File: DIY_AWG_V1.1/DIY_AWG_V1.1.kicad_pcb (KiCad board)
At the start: 4 copper layers, 100 x 100 mm, 0 parts

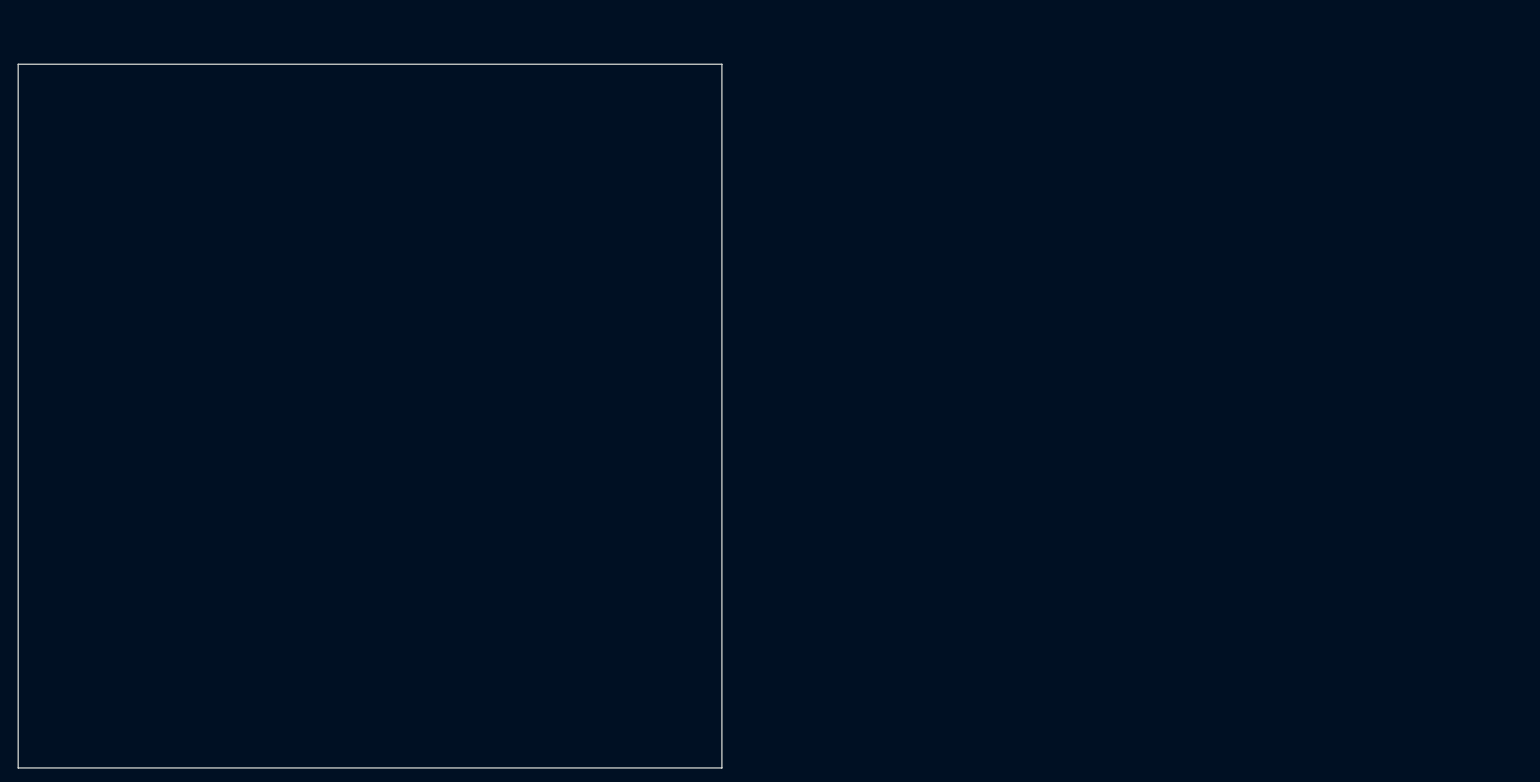
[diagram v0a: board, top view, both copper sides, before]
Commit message: Updated PCB design, uploaded necessary footprints and symbols for some components
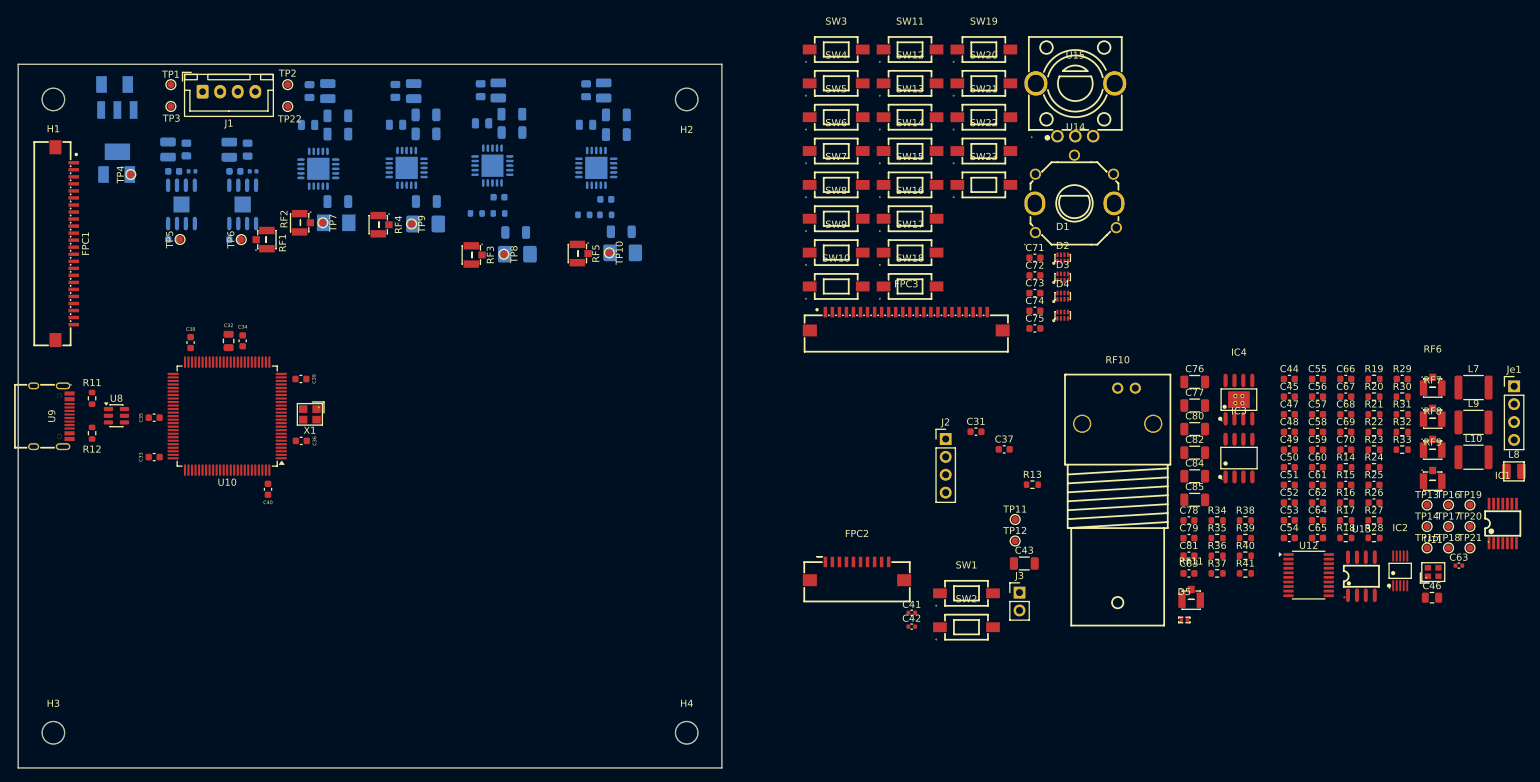
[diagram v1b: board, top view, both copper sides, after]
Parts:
- added C1: 22u, easyeda2kicad:CASE-B_3528, B.Cu at (84.2, 50.4)
- added C10: 4.7n, Capacitor_SMD:C_0402_1005Metric, B.Cu at (103.9, 62.7)
- added C11: 2.2u, Capacitor_SMD:C_0805_2012Metric, B.Cu at (111.7, 56.1)
- added C12: 22u, easyeda2kicad:CASE-B_3528, B.Cu at (84.5, 63.2)
- added C13: 10u, Capacitor_SMD:C_0603_1608Metric, B.Cu at (92.6, 72.4)
- added C14: 10u, Capacitor_SMD:C_0603_1608Metric, B.Cu at (101.3, 72.4)
- added C15: 22u, Capacitor_SMD:C_1206_3216Metric, B.Cu at (115.9, 67.0)
- added C16: 10n, Capacitor_SMD:C_0603_1608Metric, B.Cu at (138.8, 66.4)
- added C17: 22u, easyeda2kicad:CAP-SMD_L3.5-W2.8-FD, B.Cu at (115.7, 70.0)
- added C18: 22u, Capacitor_SMD:C_1206_3216Metric, B.Cu at (141.2, 71.4)
- added C19: 22u, easyeda2kicad:CAP-SMD_L3.5-W2.8-FD, B.Cu at (141.4, 74.5)
- added C2: 22u, Capacitor_SMD:C_1206_3216Metric, B.Cu at (140.7, 54.6)
- added C20: 22u, Capacitor_SMD:C_1206_3216Metric, B.Cu at (155.5, 57.5)
- added C21: 22u, Capacitor_SMD:C_1206_3216Metric, B.Cu at (128.4, 54.7)
- added C22: 22u, Capacitor_SMD:C_1206_3216Metric, B.Cu at (155.5, 54.7)
- added C23: 22u, Capacitor_SMD:C_1206_3216Metric, B.Cu at (128.4, 57.4)
- added C24: 2.2u, Capacitor_SMD:C_0805_2012Metric, B.Cu at (151.2, 56.1)
- added C25: 2.2u, Capacitor_SMD:C_0805_2012Metric, B.Cu at (124.2, 56.1)
- added C26: 22u, Capacitor_SMD:C_1206_3216Metric, B.Cu at (128.5, 67.0)
- added C27: 10n, Capacitor_SMD:C_0603_1608Metric, B.Cu at (154.0, 66.7)
- added C28: 22u, easyeda2kicad:CAP-SMD_L3.5-W2.8-FD, B.Cu at (128.4, 70.2)
- added C29: 22u, Capacitor_SMD:C_1206_3216Metric, B.Cu at (156.2, 71.3)
- added C3: 10u, Capacitor_SMD:C_0603_1608Metric, B.Cu at (92.6, 62.7)
- added C30: 22u, easyeda2kicad:CAP-SMD_L3.5-W2.8-FD, B.Cu at (156.4, 74.3)
- added C31: 100n, Capacitor_SMD:C_0603_1608Metric, F.Cu at (206.6, 99.7)
- added C32: 3.3u, Capacitor_SMD:C_0805_2012Metric, F.Cu at (100.4, 86.8)
- added C33: 100n, Capacitor_SMD:C_0603_1608Metric, F.Cu at (89.8, 103.3)
- added C34: 100n, Capacitor_SMD:C_0603_1608Metric, F.Cu at (102.4, 86.8)
- added C35: 100n, Capacitor_SMD:C_0603_1608Metric, F.Cu at (89.8, 97.7)
- added C36: 100n, Capacitor_SMD:C_0603_1608Metric, F.Cu at (110.7, 101.0)
- added C37: 100n, Capacitor_SMD:C_0603_1608Metric, F.Cu at (210.6, 102.2)
- added C38: 100n, Capacitor_SMD:C_0603_1608Metric, F.Cu at (95.0, 87.0)
- added C39: 100n, Capacitor_SMD:C_0603_1608Metric, F.Cu at (110.7, 92.2)
- added C4: 22u, Capacitor_SMD:C_1206_3216Metric, B.Cu at (140.7, 57.2)
- added C40: 10u, Capacitor_SMD:C_0603_1608Metric, F.Cu at (106.0, 107.9)
- added C41: 4.7n, Capacitor_SMD:C_0402_1005Metric, F.Cu at (197.5, 125.4)
- added C42: 4.7n, Capacitor_SMD:C_0402_1005Metric, F.Cu at (197.5, 127.4)
- added C43: 22u, Capacitor_SMD:C_1206_3216Metric, F.Cu at (213.5, 118.4)
- added C44: 20p, Capacitor_SMD:C_0603_1608Metric, F.Cu at (251.1, 92.2)
- added C45: 100n, Capacitor_SMD:C_0603_1608Metric, F.Cu at (251.1, 94.7)
- added C46: 2.2u, Capacitor_SMD:C_0805_2012Metric, F.Cu at (271.4, 123.3)
- added C47: 47p, Capacitor_SMD:C_0603_1608Metric, F.Cu at (251.1, 97.2)
- added C48: 100n, Capacitor_SMD:C_0603_1608Metric, F.Cu at (251.1, 99.8)
- added C49: 100n, Capacitor_SMD:C_0603_1608Metric, F.Cu at (251.1, 102.3)
- added C5: 10u, Capacitor_SMD:C_0603_1608Metric, B.Cu at (101.3, 62.7)
- added C50: 100n, Capacitor_SMD:C_0603_1608Metric, F.Cu at (251.1, 104.8)
- added C51: 510p, Capacitor_SMD:C_0603_1608Metric, F.Cu at (251.1, 107.3)
- added C52: 100n, Capacitor_SMD:C_0603_1608Metric, F.Cu at (251.1, 109.8)
- added C53: 10u, Capacitor_SMD:C_0603_1608Metric, F.Cu at (251.1, 112.3)
- added C54: 39p, Capacitor_SMD:C_0603_1608Metric, F.Cu at (251.1, 114.8)
- added C55: 100n, Capacitor_SMD:C_0603_1608Metric, F.Cu at (255.1, 92.2)
- added C56: 10u, Capacitor_SMD:C_0603_1608Metric, F.Cu at (255.1, 94.7)
- added C57: 510p, Capacitor_SMD:C_0603_1608Metric, F.Cu at (255.1, 97.2)
- added C58: 75p, Capacitor_SMD:C_0603_1608Metric, F.Cu at (255.1, 99.8)
- added C59: 10n, Capacitor_SMD:C_0603_1608Metric, F.Cu at (255.1, 102.3)
- added C6: 4.7n, Capacitor_SMD:C_0402_1005Metric, B.Cu at (95.2, 62.7)
- added C60: 24p, Capacitor_SMD:C_0603_1608Metric, F.Cu at (255.1, 104.8)
- added C61: 10n, Capacitor_SMD:C_0603_1608Metric, F.Cu at (255.1, 107.3)
- added C62: 82p, Capacitor_SMD:C_0603_1608Metric, F.Cu at (255.1, 109.8)
- added C63: 8.2p, Capacitor_SMD:C_0402_1005Metric, F.Cu at (275.2, 118.7)
- added C64: 68p, Capacitor_SMD:C_0603_1608Metric, F.Cu at (255.1, 112.3)
- added C65: 10u, Capacitor_SMD:C_0603_1608Metric, F.Cu at (255.1, 114.8)
- added C66: 10u, Capacitor_SMD:C_0603_1608Metric, F.Cu at (259.2, 92.2)
- added C67: 100n, Capacitor_SMD:C_0603_1608Metric, F.Cu at (259.2, 94.7)
- added C68: 100n, Capacitor_SMD:C_0603_1608Metric, F.Cu at (259.2, 97.2)
- added C69: 10u, Capacitor_SMD:C_0603_1608Metric, F.Cu at (259.2, 99.8)
- added C7: 22u, Capacitor_SMD:C_1206_3216Metric, B.Cu at (115.9, 57.4)
- added C70: 10u, Capacitor_SMD:C_0603_1608Metric, F.Cu at (259.2, 102.3)
- added C71: 100n, Capacitor_SMD:C_0603_1608Metric, F.Cu at (215.0, 75.0)
- added C72: 100n, Capacitor_SMD:C_0603_1608Metric, F.Cu at (215.0, 77.5)
- added C73: 100n, Capacitor_SMD:C_0603_1608Metric, F.Cu at (215.0, 80.0)
- added C74: 100n, Capacitor_SMD:C_0603_1608Metric, F.Cu at (215.0, 82.5)
- added C75: 100n, Capacitor_SMD:C_0603_1608Metric, F.Cu at (215.0, 85.0)
- added C76: 22u, Capacitor_SMD:C_1206_3216Metric, F.Cu at (237.7, 92.6)
- added C77: 22u, Capacitor_SMD:C_1206_3216Metric, F.Cu at (237.7, 96.0)
- added C78: 100n, Capacitor_SMD:C_0603_1608Metric, F.Cu at (236.9, 112.3)
- added C79: 100n, Capacitor_SMD:C_0603_1608Metric, F.Cu at (236.9, 114.8)
- added C8: 2.2u, Capacitor_SMD:C_0805_2012Metric, B.Cu at (136.4, 55.9)
- added C80: 22u, Capacitor_SMD:C_1206_3216Metric, F.Cu at (237.7, 99.3)
- added C81: 100n, Capacitor_SMD:C_0603_1608Metric, F.Cu at (236.9, 117.3)
- added C82: 22u, Capacitor_SMD:C_1206_3216Metric, F.Cu at (237.7, 102.7)
- added C83: 100n, Capacitor_SMD:C_0603_1608Metric, F.Cu at (236.9, 119.9)
- added C84: 22u, Capacitor_SMD:C_1206_3216Metric, F.Cu at (237.7, 106.0)
- added C85: 22u, Capacitor_SMD:C_1206_3216Metric, F.Cu at (237.7, 109.4)
- added C9: 22u, Capacitor_SMD:C_1206_3216Metric, B.Cu at (115.9, 54.8)
- added D1: RL20108Q0332LC, easyeda2kicad:DFN-8_L2.0-W1.0-P0.50-BL, F.Cu at (218.9, 75.0)
- added D2: RL20108Q0332LC, easyeda2kicad:DFN-8_L2.0-W1.0-P0.50-BL, F.Cu at (218.9, 77.7)
- added D3: RL20108Q0332LC, easyeda2kicad:DFN-8_L2.0-W1.0-P0.50-BL, F.Cu at (218.9, 80.5)
- added D4: RL20108Q0332LC, easyeda2kicad:DFN-8_L2.0-W1.0-P0.50-BL, F.Cu at (218.9, 83.2)
- added D5: TPESD1221P, easyeda2kicad:DFN1006-2L-BI, F.Cu at (236.2, 126.5)
- added FPC1: FC-10A24P11H20, easyeda2kicad:FPC-SMD_24P-P1.00_FC-10A24P11H20, F.Cu at (77.1, 73.0)
- added FPC2: XW1020012-100R-002, easyeda2kicad:FPC-SMD_10P-P1.00_XW1020012-100R-001, F.Cu at (189.7, 119.5)
- added FPC3: FC-10A24P11H20, easyeda2kicad:FPC-SMD_24P-P1.00_FC-10A24P11H20, F.Cu at (196.7, 84.0)
- added H1: MountingHole, MountingHole:MountingHole_3.2mm_M3, F.Cu at (75.5, 52.5)
- added H2: MountingHole, MountingHole:MountingHole_3.2mm_M3, F.Cu at (165.5, 52.5)
- added H3: MountingHole, MountingHole:MountingHole_3.2mm_M3, F.Cu at (75.5, 142.5)
- added H4: MountingHole, MountingHole:MountingHole_3.2mm_M3, F.Cu at (165.5, 142.5)
- added IC1: TLV3544IPWR, easyeda2kicad:TSSOP-14_L5.0-W4.4-P0.65-LS6.4-BL, F.Cu at (281.5, 112.8)
- added IC2: ADG704BRMZ-REEL7, easyeda2kicad:MSOP-10_L3.0-W3.0-P0.50-LS5.0-BL, F.Cu at (266.9, 119.5)
- added IC3: LMH6505MAX, easyeda2kicad:SOP-8_L4.9-W3.9-P1.27-LS6.0-BL, F.Cu at (244.0, 103.5)
- added IC4: THS3091DDAR, easyeda2kicad:SOIC-8_L4.9-W3.9-P1.27-LS6.0-BL-EP, F.Cu at (244.0, 95.2)
- added J1: Conn_01x04_Socket, Connector_JST:JST_XH_B4B-XH-A_1x04_P2.50mm_Vertical, F.Cu at (96.7, 51.4)
- added J2: Conn_01x04_Pin, Connector_PinHeader_2.54mm:PinHeader_1x04_P2.54mm_Vertical, F.Cu at (202.3, 100.8)
- added J3: Conn_01x02_Pin, Connector_PinHeader_2.54mm:PinHeader_1x02_P2.54mm_Vertical, F.Cu at (212.8, 122.6)
- added Je1: Conn_01x04_Pin, Connector_PinHeader_2.54mm:PinHeader_1x04_P2.54mm_Vertical, F.Cu at (283.1, 93.3)
- added L1: 1.5u, Inductor_SMD:L_1008_2520Metric, B.Cu at (91.8, 59.6)
- added L10: 1.8u, Inductor_SMD:L_1812_4532Metric, F.Cu at (277.3, 103.3)
- added L2: 0.33u, Inductor_SMD:L_1008_2520Metric, B.Cu at (138.7, 51.2)
- added L3: 1.5u, Inductor_SMD:L_1008_2520Metric, B.Cu at (100.5, 59.6)
- added L4: 0.47u, Inductor_SMD:L_1008_2520Metric, B.Cu at (114.5, 51.3)
- added L5: 0.33u, Inductor_SMD:L_1008_2520Metric, B.Cu at (153.7, 51.2)
- added L6: 0.47u, Inductor_SMD:L_1008_2520Metric, B.Cu at (126.7, 51.3)
- added L7: 1u, Inductor_SMD:L_1812_4532Metric, F.Cu at (277.3, 93.4)
- added L8: 2.7u, easyeda2kicad:L_1008_2520_SLQW2520, F.Cu at (283.1, 105.4)
- added L9: 1.5u, Inductor_SMD:L_1812_4532Metric, F.Cu at (277.3, 98.4)
- added R1: 400m, Resistor_SMD:R_0805_2012Metric, B.Cu at (94.4, 59.6)
- added R10: 49.9k, Resistor_SMD:R_0603_1608Metric, B.Cu at (150.9, 68.9)
- added R11: 5.1k, Resistor_SMD:R_0603_1608Metric, F.Cu at (81.0, 95.0)
- added R12: 5.1k, Resistor_SMD:R_0603_1608Metric, F.Cu at (81.0, 99.9)
- added R13: 5.1k, Resistor_SMD:R_0603_1608Metric, F.Cu at (214.6, 107.2)
- added R14: 0, Resistor_SMD:R_0603_1608Metric, F.Cu at (259.2, 104.8)
- added R15: 200, Capacitor_SMD:C_0603_1608Metric, F.Cu at (259.2, 107.3)
- added R16: 10k, Resistor_SMD:R_0603_1608Metric, F.Cu at (259.2, 109.8)
- added R17: 1k, Resistor_SMD:R_0603_1608Metric, F.Cu at (259.2, 112.3)
- added R18: 0, Resistor_SMD:R_0603_1608Metric, F.Cu at (259.2, 114.8)
- added R19: 50, Resistor_SMD:R_0603_1608Metric, F.Cu at (263.2, 92.2)
- added R2: 400m, Resistor_SMD:R_0805_2012Metric, B.Cu at (136.2, 51.2)
- added R20: 9.53, Resistor_SMD:R_0603_1608Metric, F.Cu at (263.2, 94.7)
- added R21: 40.2, Resistor_SMD:R_0603_1608Metric, F.Cu at (263.2, 97.2)
- added R22: 0, Resistor_SMD:R_0603_1608Metric, F.Cu at (263.2, 99.8)
- added R23: 9.53, Resistor_SMD:R_0603_1608Metric, F.Cu at (263.2, 102.3)
- added R24: 0, Resistor_SMD:R_0603_1608Metric, F.Cu at (263.2, 104.8)
- added R25: 6.8k, Capacitor_SMD:C_0603_1608Metric, F.Cu at (263.2, 107.3)
- added R26: 200, Capacitor_SMD:C_0603_1608Metric, F.Cu at (263.2, 109.8)
- added R27: 20k, Resistor_SMD:R_0603_1608Metric, F.Cu at (263.2, 112.3)
- added R28: 1k, Resistor_SMD:R_0603_1608Metric, F.Cu at (263.2, 114.8)
- added R29: 200, Capacitor_SMD:C_0603_1608Metric, F.Cu at (267.2, 92.2)
- added R3: 400m, Resistor_SMD:R_0805_2012Metric, B.Cu at (103.1, 59.6)
- added R30: 20k, Resistor_SMD:R_0603_1608Metric, F.Cu at (267.2, 94.7)
- added R31: 30k, Resistor_SMD:R_0603_1608Metric, F.Cu at (267.2, 97.2)
- added R32: 10k, Resistor_SMD:R_0603_1608Metric, F.Cu at (267.2, 99.8)
- added R33: 20k, Resistor_SMD:R_0603_1608Metric, F.Cu at (267.2, 102.3)
- added R34: 1.3k, Resistor_SMD:R_0603_1608Metric, F.Cu at (240.9, 112.3)
- added R35: 2k, Resistor_SMD:R_0603_1608Metric, F.Cu at (240.9, 114.8)
- added R36: 237, Resistor_SMD:R_0603_1608Metric, F.Cu at (240.9, 117.3)
- added R37: 249, Resistor_SMD:R_0603_1608Metric, F.Cu at (240.9, 119.9)
- added R38: 1k, Resistor_SMD:R_0603_1608Metric, F.Cu at (244.9, 112.3)
- added R39: 1k, Resistor_SMD:R_0603_1608Metric, F.Cu at (244.9, 114.8)
- added R4: 400m, Resistor_SMD:R_0805_2012Metric, B.Cu at (111.9, 51.3)
- added R40: 50, Resistor_SMD:R_0603_1608Metric, F.Cu at (244.9, 117.3)
- added R41: 0, Resistor_SMD:R_0603_1608Metric, F.Cu at (244.9, 119.9)
- added R5: 162k, Resistor_SMD:R_0603_1608Metric, B.Cu at (138.8, 68.7)
- added R6: 21.5k, Resistor_SMD:R_0603_1608Metric, B.Cu at (135.6, 68.7)
- added R7: 400m, Resistor_SMD:R_0805_2012Metric, B.Cu at (151.2, 51.2)
- added R8: 400m, Resistor_SMD:R_0805_2012Metric, B.Cu at (124.1, 51.3)
- added R9: 162k, Resistor_SMD:R_0603_1608Metric, B.Cu at (154.0, 68.9)
- added RF1: IPEX-01, easyeda2kicad:IPEX-SMD_3P-L2.6-W2.6-LS3.0_YUANDI_RF-001, F.Cu at (105.1, 72.4)
- added RF10: KH-BNC50-3511, easyeda2kicad:ANT-TH_KH-BNC50-3511, F.Cu at (226.7, 96.1)
- added RF11: IPEX-01, easyeda2kicad:IPEX-SMD_3P-L2.6-W2.6-LS3.0_YUANDI_RF-001, F.Cu at (237.2, 122.9)
- added RF2: IPEX-01, easyeda2kicad:IPEX-SMD_3P-L2.6-W2.6-LS3.0_YUANDI_RF-001, F.Cu at (111.3, 70.0)
- added RF3: IPEX-01, easyeda2kicad:IPEX-SMD_3P-L2.6-W2.6-LS3.0_YUANDI_RF-001, F.Cu at (135.6, 74.6)
- added RF4: IPEX-01, easyeda2kicad:IPEX-SMD_3P-L2.6-W2.6-LS3.0_YUANDI_RF-001, F.Cu at (122.4, 70.3)
- added RF5: IPEX-01, easyeda2kicad:IPEX-SMD_3P-L2.6-W2.6-LS3.0_YUANDI_RF-001, F.Cu at (150.7, 74.4)
- added RF6: IPEX-01, easyeda2kicad:IPEX-SMD_3P-L2.6-W2.6-LS3.0_YUANDI_RF-001, F.Cu at (271.5, 92.8)
- added RF7: IPEX-01, easyeda2kicad:IPEX-SMD_3P-L2.6-W2.6-LS3.0_YUANDI_RF-001, F.Cu at (271.5, 97.2)
- added RF8: IPEX-01, easyeda2kicad:IPEX-SMD_3P-L2.6-W2.6-LS3.0_YUANDI_RF-001, F.Cu at (271.5, 101.6)
- added RF9: IPEX-01, easyeda2kicad:IPEX-SMD_3P-L2.6-W2.6-LS3.0_YUANDI_RF-001, F.Cu at (271.5, 106.0)
- added SW1: SW_Push, easyeda2kicad:SW-SMD_L6.1-W3.5-LS8.6, F.Cu at (205.3, 122.7)
- added SW10: SW_Push, easyeda2kicad:SW-SMD_L6.1-W3.5-LS8.6, F.Cu at (186.7, 79.1)
- added SW11: SW_Push, easyeda2kicad:SW-SMD_L6.1-W3.5-LS8.6, F.Cu at (197.2, 45.4)
- added SW12: SW_Push, easyeda2kicad:SW-SMD_L6.1-W3.5-LS8.6, F.Cu at (197.2, 50.2)
- added SW13: SW_Push, easyeda2kicad:SW-SMD_L6.1-W3.5-LS8.6, F.Cu at (197.2, 55.0)
- added SW14: SW_Push, easyeda2kicad:SW-SMD_L6.1-W3.5-LS8.6, F.Cu at (197.2, 59.8)
- added SW15: SW_Push, easyeda2kicad:SW-SMD_L6.1-W3.5-LS8.6, F.Cu at (197.2, 64.6)
- added SW16: SW_Push, easyeda2kicad:SW-SMD_L6.1-W3.5-LS8.6, F.Cu at (197.2, 69.5)
- added SW17: SW_Push, easyeda2kicad:SW-SMD_L6.1-W3.5-LS8.6, F.Cu at (197.2, 74.3)
- added SW18: SW_Push, easyeda2kicad:SW-SMD_L6.1-W3.5-LS8.6, F.Cu at (197.2, 79.1)
- added SW19: SW_Push, easyeda2kicad:SW-SMD_L6.1-W3.5-LS8.6, F.Cu at (207.7, 45.4)
- added SW2: SW_Push, easyeda2kicad:SW-SMD_L6.1-W3.5-LS8.6, F.Cu at (205.3, 127.5)
- added SW20: SW_Push, easyeda2kicad:SW-SMD_L6.1-W3.5-LS8.6, F.Cu at (207.7, 50.2)
- added SW21: SW_Push, easyeda2kicad:SW-SMD_L6.1-W3.5-LS8.6, F.Cu at (207.7, 55.0)
- added SW22: SW_Push, easyeda2kicad:SW-SMD_L6.1-W3.5-LS8.6, F.Cu at (207.7, 59.8)
- added SW23: SW_Push, easyeda2kicad:SW-SMD_L6.1-W3.5-LS8.6, F.Cu at (207.7, 64.6)
- added SW3: SW_Push, easyeda2kicad:SW-SMD_L6.1-W3.5-LS8.6, F.Cu at (186.7, 45.4)
- added SW4: SW_Push, easyeda2kicad:SW-SMD_L6.1-W3.5-LS8.6, F.Cu at (186.7, 50.2)
- added SW5: SW_Push, easyeda2kicad:SW-SMD_L6.1-W3.5-LS8.6, F.Cu at (186.7, 55.0)
- added SW6: SW_Push, easyeda2kicad:SW-SMD_L6.1-W3.5-LS8.6, F.Cu at (186.7, 59.8)
- added SW7: SW_Push, easyeda2kicad:SW-SMD_L6.1-W3.5-LS8.6, F.Cu at (186.7, 64.6)
- added SW8: SW_Push, easyeda2kicad:SW-SMD_L6.1-W3.5-LS8.6, F.Cu at (186.7, 69.5)
- added SW9: SW_Push, easyeda2kicad:SW-SMD_L6.1-W3.5-LS8.6, F.Cu at (186.7, 74.3)
- added TP1: TestPoint, TestPoint:TestPoint_Pad_D1.0mm, F.Cu at (92.2, 50.4)
- added TP10: TestPoint, TestPoint:TestPoint_Pad_D1.0mm, F.Cu at (154.5, 74.3)
- added TP11: TestPoint, TestPoint:TestPoint_Pad_D1.0mm, F.Cu at (212.2, 112.2)
- added TP12: TestPoint, TestPoint:TestPoint_Pad_D1.0mm, F.Cu at (212.2, 115.2)
- added TP13: TestPoint, TestPoint:TestPoint_Pad_D1.0mm, F.Cu at (270.7, 110.1)
- added TP14: TestPoint, TestPoint:TestPoint_Pad_D1.0mm, F.Cu at (270.7, 113.2)
- added TP15: TestPoint, TestPoint:TestPoint_Pad_D1.0mm, F.Cu at (270.7, 116.2)
- added TP16: TestPoint, TestPoint:TestPoint_Pad_D1.0mm, F.Cu at (273.8, 110.1)
- added TP17: TestPoint, TestPoint:TestPoint_Pad_D1.0mm, F.Cu at (273.8, 113.2)
- added TP18: TestPoint, TestPoint:TestPoint_Pad_D1.0mm, F.Cu at (273.8, 116.2)
- added TP19: TestPoint, TestPoint:TestPoint_Pad_D1.0mm, F.Cu at (276.8, 110.1)
- added TP2: TestPoint, TestPoint:TestPoint_Pad_D1.0mm, F.Cu at (108.8, 50.4)
- added TP20: TestPoint, TestPoint:TestPoint_Pad_D1.0mm, F.Cu at (276.8, 113.2)
- added TP21: TestPoint, TestPoint:TestPoint_Pad_D1.0mm, F.Cu at (276.8, 116.2)
- added TP22: TestPoint, TestPoint:TestPoint_Pad_D1.0mm, F.Cu at (108.8, 53.5)
- added TP3: TestPoint, TestPoint:TestPoint_Pad_D1.0mm, F.Cu at (92.2, 53.5)
- added TP4: TestPoint, TestPoint:TestPoint_Pad_D1.0mm, F.Cu at (86.5, 63.2)
- added TP5: TestPoint, TestPoint:TestPoint_Pad_D1.0mm, F.Cu at (93.5, 72.4)
- added TP6: TestPoint, TestPoint:TestPoint_Pad_D1.0mm, F.Cu at (102.2, 72.4)
- added TP7: TestPoint, TestPoint:TestPoint_Pad_D1.0mm, F.Cu at (113.8, 70.0)
- added TP8: TestPoint, TestPoint:TestPoint_Pad_D1.0mm, F.Cu at (139.5, 74.5)
- added TP9: TestPoint, TestPoint:TestPoint_Pad_D1.0mm, F.Cu at (126.4, 70.2)
- added U1: AMS1117-3.3, easyeda2kicad:SOT-223-3_L6.5-W3.4-P2.30-LS7.0-BR, B.Cu at (84.6, 57.0)
- added U10: STM32G473VETx, Package_QFP:LQFP-100_14x14mm_P0.5mm, F.Cu at (100.2, 97.5)
- added U11: 8121H-50.000NK33DRL, easyeda2kicad:OSC-SMD_4P-L2.0-W1.6-BL_SIT8008BI-72-33E-54.000000, F.Cu at (271.6, 119.7)
- added U12: AD9834, Package_SO:TSSOP-20_4.4x6.5mm_P0.65mm, F.Cu at (253.9, 120.1)
- added U13: OPA2171AIDR, easyeda2kicad:SOIC-8_L5.0-W4.0-P1.27-LS6.0-BL, F.Cu at (261.4, 120.3)
- added U14: EC12D1564402, easyeda2kicad:SW-TH_EC12D1564402, F.Cu at (220.8, 65.9)
- added U15: EC12E2430404, easyeda2kicad:SW-TH_ALPSALPINE_EC12EXXXX, F.Cu at (220.7, 54.0)
- added U2: ADP7118ARDZ-3.3-R7, easyeda2kicad:SOIC-8_L4.9-W3.9-P1.27-LS6.0-BL-EP2.3, B.Cu at (93.7, 67.4)
- added U3: ADP7118ARDZ-3.3-R7, easyeda2kicad:SOIC-8_L4.9-W3.9-P1.27-LS6.0-BL-EP2.3, B.Cu at (102.4, 67.4)
- added U4: TPS7A3301RGWR, easyeda2kicad:VQFN-20_L5.0-W5.0-P0.65-TL-EP, B.Cu at (137.9, 61.9)
- added U5: TPS7A4701RGWR, easyeda2kicad:VQFN-20_L5.0-W5.0-P0.65-TL-EP, B.Cu at (113.2, 62.4)
- added U6: TPS7A3301RGWR, easyeda2kicad:VQFN-20_L5.0-W5.0-P0.65-TL-EP, B.Cu at (152.7, 62.2)
- added U7: TPS7A4701RGWR, easyeda2kicad:VQFN-20_L5.0-W5.0-P0.65-TL-EP, B.Cu at (125.7, 62.2)
- added U8: USBLC6-2SC6, Package_TO_SOT_SMD:SOT-23-6, F.Cu at (84.5, 97.5)
- added U9: 161N-4BVS11, easyeda2kicad:USB-C-SMD_HANELECTRICITY_161N-4XVS11, F.Cu at (75.2, 97.5)
- added X1: SX2M8.000B10F20TNN, easyeda2kicad:OSC-SMD_4P-L2.5-W2.0-BL, F.Cu at (112.0, 97.2)

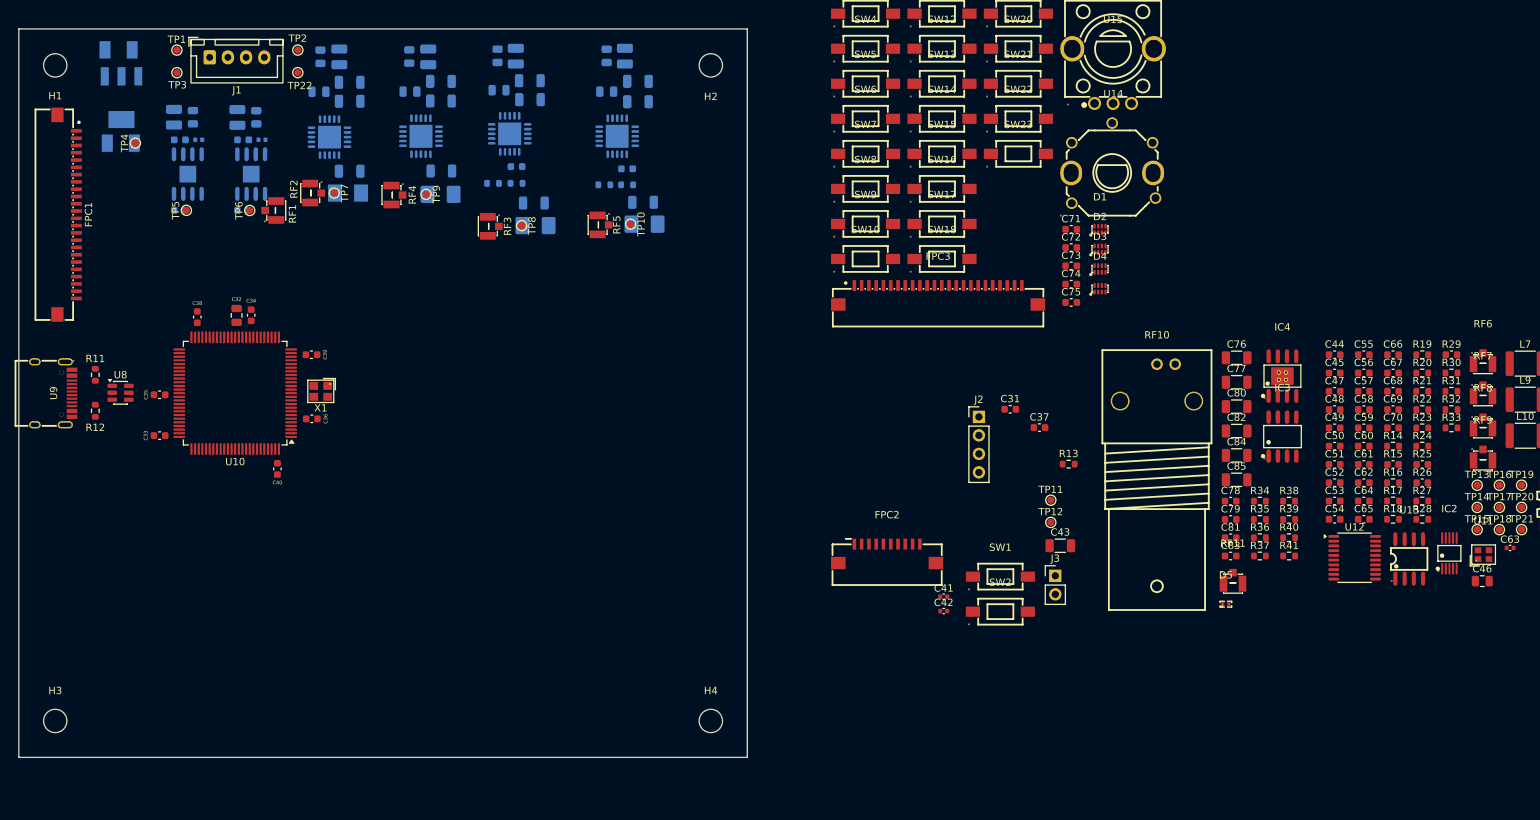
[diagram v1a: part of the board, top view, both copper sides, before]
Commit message: Edited the electrical schematics, PCB design
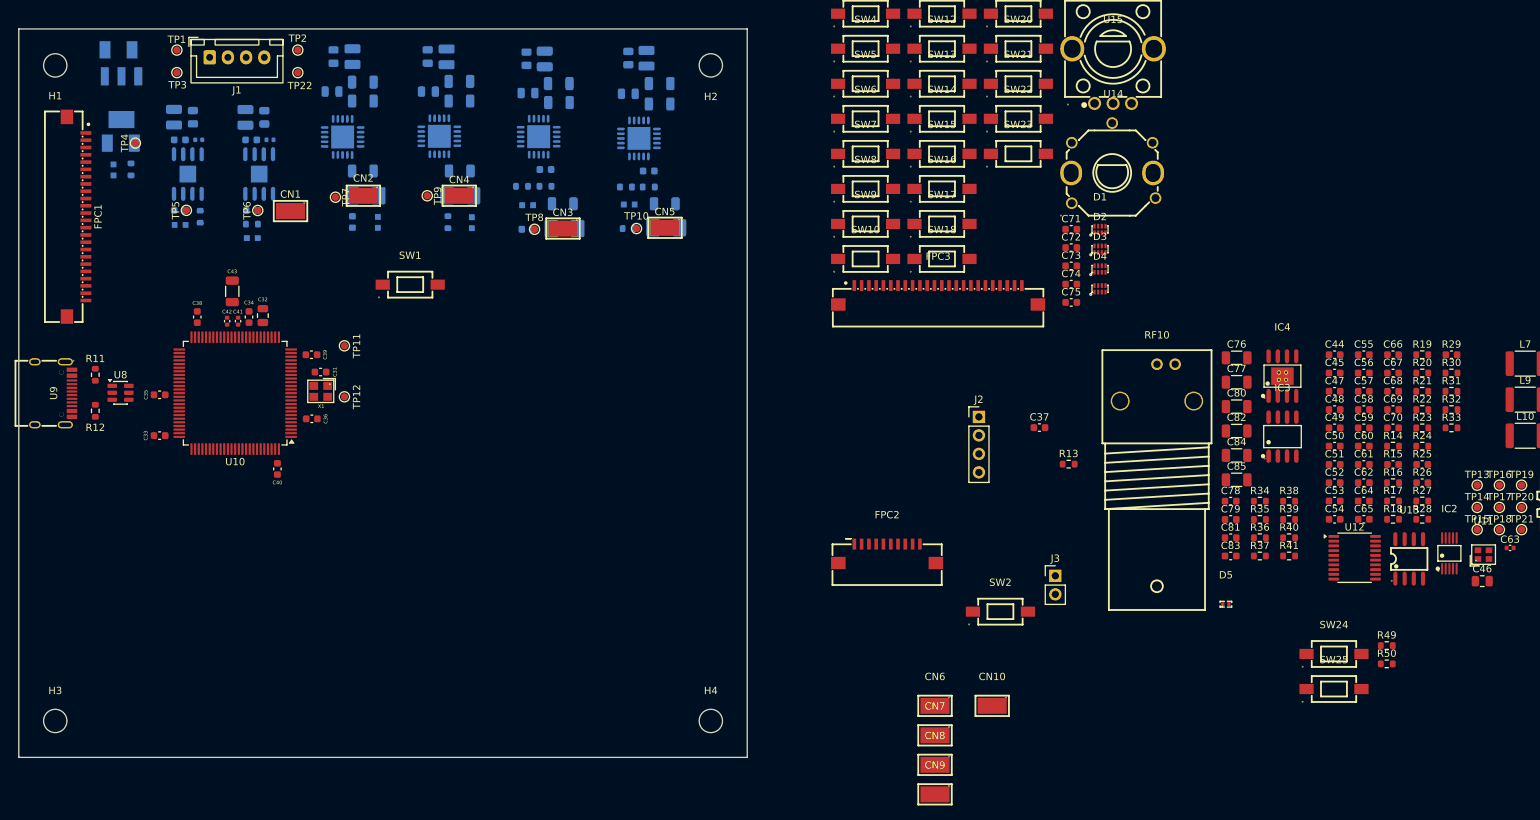
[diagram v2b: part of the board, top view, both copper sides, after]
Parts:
- removed RF1, RF11, RF2, RF3, RF4, RF5, RF6, RF7, RF8, RF9: IPEX-01, easyeda2kicad:IPEX-SMD_3P-L2.6-W2.6-LS3.0_YUANDI_RF-001
- added CN1: RH-5019, easyeda2kicad:TESTPOINT-SMD_L3.8-W2.0_RH-5019, F.Cu at (107.8, 72.5)
- added CN10: RH-5019, easyeda2kicad:TESTPOINT-SMD_L3.8-W2.0_RH-5019, F.Cu at (204.1, 140.4)
- added CN2: RH-5019, easyeda2kicad:TESTPOINT-SMD_L3.8-W2.0_RH-5019, F.Cu at (117.8, 70.4)
- added CN3: RH-5019, easyeda2kicad:TESTPOINT-SMD_L3.8-W2.0_RH-5019, F.Cu at (145.2, 74.9)
- added CN4: RH-5019, easyeda2kicad:TESTPOINT-SMD_L3.8-W2.0_RH-5019, F.Cu at (131.0, 70.4)
- added CN5: RH-5019, easyeda2kicad:TESTPOINT-SMD_L3.8-W2.0_RH-5019, F.Cu at (159.2, 74.8)
- added CN6: RH-5019, easyeda2kicad:TESTPOINT-SMD_L3.8-W2.0_RH-5019, F.Cu at (196.3, 140.4)
- added CN7: RH-5019, easyeda2kicad:TESTPOINT-SMD_L3.8-W2.0_RH-5019, F.Cu at (196.3, 144.5)
- added CN8: RH-5019, easyeda2kicad:TESTPOINT-SMD_L3.8-W2.0_RH-5019, F.Cu at (196.3, 148.5)
- added CN9: RH-5019, easyeda2kicad:TESTPOINT-SMD_L3.8-W2.0_RH-5019, F.Cu at (196.3, 152.6)
- added LED1: XL-1608SURC-06, easyeda2kicad:LED0603-RD_RED, B.Cu at (83.5, 66.8)
- added LED2: XL-1608SURC-06, easyeda2kicad:LED0603-RD_RED, B.Cu at (92.7, 74.4)
- added LED3: XL-1608SURC-06, easyeda2kicad:LED0603-RD_RED, B.Cu at (102.5, 76.2)
- added LED4: XL-1608SURC-06, easyeda2kicad:LED0603-RD_RED, B.Cu at (119.8, 74.0)
- added LED5: XL-1608SURC-06, easyeda2kicad:LED0603-RD_RED, B.Cu at (140.3, 71.7)
- added LED6: XL-1608SURC-06, easyeda2kicad:LED0603-RD_RED, B.Cu at (132.7, 74.1)
- added LED7: XL-1608SURC-06, easyeda2kicad:LED0603-RD_RED, B.Cu at (154.3, 71.6)
- added R42: 1k, Resistor_SMD:R_0603_1608Metric, B.Cu at (85.9, 66.8)
- added R43: 1k, Resistor_SMD:R_0603_1608Metric, B.Cu at (95.4, 73.3)
- added R44: 1k, Resistor_SMD:R_0603_1608Metric, B.Cu at (102.5, 74.3)
- added R45: 6.8k, Capacitor_SMD:C_0603_1608Metric, B.Cu at (116.3, 74.0)
- added R46: 6.8k, Capacitor_SMD:C_0603_1608Metric, B.Cu at (140.3, 75.0)
- added R47: 2k, Resistor_SMD:R_0603_1608Metric, B.Cu at (129.4, 74.0)
- added R48: 2k, Resistor_SMD:R_0603_1608Metric, B.Cu at (154.2, 74.9)
- added R49: 5.1k, Resistor_SMD:R_0603_1608Metric, F.Cu at (258.3, 132.2)
- added R50: 5.1k, Resistor_SMD:R_0603_1608Metric, F.Cu at (258.3, 134.7)
- added SW24: SW_Push, easyeda2kicad:SW-SMD_L6.1-W3.5-LS8.6, F.Cu at (251.0, 133.3)
- added SW25: SW_Push, easyeda2kicad:SW-SMD_L6.1-W3.5-LS8.6, F.Cu at (251.0, 138.1)
- moved C43 118.9 mm to (99.8, 83.5), turned to 90 degrees
- moved C42 106.1 mm to (99.1, 87.6), turned to 90 degrees
- moved C41 104.0 mm to (100.6, 87.6), turned to 90 degrees
- moved TP11 99.3 mm to (115.2, 91.0), turned to -90 degrees
- moved TP12 98.5 mm to (115.2, 98.0), turned to -90 degrees
- moved C31 94.8 mm to (111.9, 94.6), turned to 180 degrees
- moved SW1 90.4 mm to (124.2, 82.6)
- moved C16 4.00 mm to (142.8, 66.8)
- moved R5 4.00 mm to (142.8, 69.1)
- moved C19 4.00 mm to (145.4, 74.9)
- moved C2 4.00 mm to (144.6, 55.0)
- moved C4 4.00 mm to (144.7, 57.6)
- moved C8 4.00 mm to (140.4, 56.3)
- moved L2 4.00 mm to (142.7, 51.6)
- moved R2 4.00 mm to (140.2, 51.6)
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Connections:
- U10 pad 47: unconnected-(U10-PB10-Pad47) -> Net-(U10-PB10)
- U10 pad 50: unconnected-(U10-PB11-Pad50) -> Net-(U10-PB11)

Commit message: Edited the PCB design
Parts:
- moved J1 196.3 mm to (87.1, 82.2)
- moved SW24 170.1 mm to (81.0, 128.0)
- moved SW25 170.1 mm to (81.0, 134.0)
- moved R49 169.3 mm to (89.0, 128.0)
- moved R50 169.3 mm to (89.0, 134.0)
- moved U11 147.3 mm to (124.2, 118.8)
- moved TP14 142.9 mm to (127.9, 118.3)
- moved TP13 136.1 mm to (134.9, 118.4)
- moved C55 133.1 mm to (123.3, 110.8), turned to -90 degrees
- moved C45 132.2 mm to (121.2, 118.9), turned to 90 degrees
- moved C56 130.8 mm to (125.3, 110.8), turned to -90 degrees
- moved C50 130.3 mm to (121.2, 114.4), turned to 90 degrees
- moved TP15 130.1 mm to (141.1, 127.1)
- moved TP16 129.0 mm to (145.9, 127.4)
- moved C52 127.9 mm to (123.3, 114.4), turned to 90 degrees
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- renumbered TP7 to +10V, TP2 to +12V, TP6 to +3V3, TP5 to +3V3, TP4 to +3V3, TP1 to +5V, TP9 to +5V, TP8 to -10V, TP22 to -12V, TP10 to -5V, TP3 to GND, Je1 to J1

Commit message: Updated schematic PCB design
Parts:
- added CN11: RH-5019, easyeda2kicad:TESTPOINT-SMD_L3.8-W2.0_RH-5019, F.Cu at (138.6, 139.3)
- added CN12: RH-5019, easyeda2kicad:TESTPOINT-SMD_L3.8-W2.0_RH-5019, F.Cu at (138.6, 126.1)
- added TP11: TestPoint, TestPoint:TestPoint_Pad_D1.0mm, F.Cu at (119.9, 63.4)
- added TP12: TestPoint, TestPoint:TestPoint_Pad_D1.0mm, F.Cu at (146.2, 67.9)
- added TP14: TestPoint, TestPoint:TestPoint_Pad_D1.0mm, F.Cu at (132.9, 63.4)
- added TP16: TestPoint, TestPoint:TestPoint_Pad_D1.0mm, F.Cu at (160.3, 67.8)
- added TP8: TestPoint, TestPoint:TestPoint_Pad_D1.0mm, F.Cu at (107.8, 65.5)
- LED1, LED2, LED3, LED4, LED5, LED6, LED7: moved to F.Cu
- moved TP26 179.9 mm to (104.4, 164.7)
- moved TP27 178.0 mm to (104.6, 161.1)
- moved TP25 176.3 mm to (106.1, 154.1)
- moved C66 167.3 mm to (95.8, 128.5)
- moved C68 167.0 mm to (101.1, 151.0)
- moved C69 167.0 mm to (101.1, 153.5)
- moved C70 167.0 mm to (101.1, 156.0)
- moved R42 166.9 mm to (111.3, 161.9)
- moved R41 166.0 mm to (111.6, 157.5)
- moved C67 165.8 mm to (95.8, 123.3)
- moved R40 165.2 mm to (111.7, 153.1)
- moved R39 165.0 mm to (111.4, 149.1)
- moved U13 160.8 mm to (100.8, 127.8)
- moved C65 159.7 mm to (95.8, 125.9)
- moved IC1 159.1 mm to (124.1, 89.3), turned to -90 degrees
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- renumbered CN8 to CN6, CN9 to CN8, CN6 to CN9, J1 to Je1, R45 to R10, R46 to R11, R7 to R12, R8 to R13, R9 to R14, R10 to R15, R47 to R16, R48 to R17, R11 to R18, R12 to R19, R13 to R20, R49 to R21, R50 to R22, R14 to R23, R15 to R24, R16 to R25, R17 to R26, R18 to R27, R19 to R28, R20 to R29, R21 to R30, R22 to R31, R23 to R32, R24 to R33, R25 to R34, R26 to R35, R27 to R36, R28 to R37, R29 to R38, R30 to R39, R31 to R40, R32 to R41, R33 to R42, R34 to R43, R35 to R44, R36 to R45, R37 to R46, R38 to R47, R39 to R48, R40 to R49, R42 to R5, R41 to R50, R43 to R6, R44 to R7, R5 to R8, R6 to R9, RF10 to RF1, SW8 to SW10, SW9 to SW11, SW10 to SW12, SW11 to SW13, SW12 to SW14, SW13 to SW15, SW14 to SW16, SW15 to SW17, SW16 to SW18, SW17 to SW19, SW18 to SW20, SW19 to SW21, SW20 to SW22, SW21 to SW23, SW22 to SW24, SW23 to SW25, SW24 to SW3, SW25 to SW4, SW3 to SW5, SW4 to SW6, SW5 to SW7, SW6 to SW8, SW7 to SW9, +5V to TP1, -10V to TP10, +5V to TP13, -5V to TP15, TP11 to TP17, TP12 to TP18, TP13 to TP19, +12V to TP2, TP14 to TP20, TP15 to TP21, TP16 to TP22, TP17 to TP23, TP18 to TP24, TP19 to TP25, TP20 to TP26, TP21 to TP27, -12V to TP3, GND to TP4, +3V3 to TP5, +3V3 to TP6, +3V3 to TP7, +10V to TP9
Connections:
- IC1 pad 10: Net-(IC1C-INC+) -> GND
- IC1 pad 12: GND -> Net-(IC1D-IND+)
- IC1 pad 13: Net-(IC1D-IND-) -> /AD9834_DDS/REF_SIG1
- IC1 pad 14: Net-(IC1D-IND-) -> /AD9834_DDS/REF_SIG1
- IC1 pad 8: /AD9834_DDS/REF_SIG1 -> Net-(IC1C-INC-)
- IC1 pad 9: /AD9834_DDS/REF_SIG1 -> Net-(IC1C-INC-)
- R36 pad 1: Net-(IC1C-INC+) -> Net-(IC1D-IND+)
- R37 pad 1: Net-(IC1C-INC+) -> Net-(IC1D-IND+)

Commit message: Updated PCB design
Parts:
- moved R47 107.8 mm to (139.1, 92.0), turned to 90 degrees
- moved C85 102.9 mm to (137.6, 85.8), turned to 90 degrees
- moved R43 102.6 mm to (138.7, 121.5), turned to 180 degrees
- moved R44 102.3 mm to (138.7, 118.1)
- moved R45 102.2 mm to (138.7, 114.7)
- moved R50 101.8 mm to (143.9, 107.5)
- moved R48 101.1 mm to (143.9, 110.5)
- moved IC3 100.5 mm to (144.2, 115.4)
- moved C80 100.3 mm to (137.9, 109.5), turned to -90 degrees
- moved R46 99.6 mm to (143.8, 97.8), turned to -90 degrees
- moved R49 98.8 mm to (150.1, 89.4)
- moved IC4 98.8 mm to (145.2, 92.1)
- moved C84 98.6 mm to (141.2, 85.8), turned to 90 degrees
- moved C83 98.4 mm to (144.2, 86.6), turned to 90 degrees
- moved C79 96.4 mm to (140.6, 110.3), turned to -90 degrees
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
